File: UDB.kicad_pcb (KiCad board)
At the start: 4 copper layers, 18 x 16.5 mm, 14 parts, among them J1 TYPE-C-31-M12_13, J2 SM04B-SRSS-TB(LF)(SN), U1 TPD4E05U06DQAR

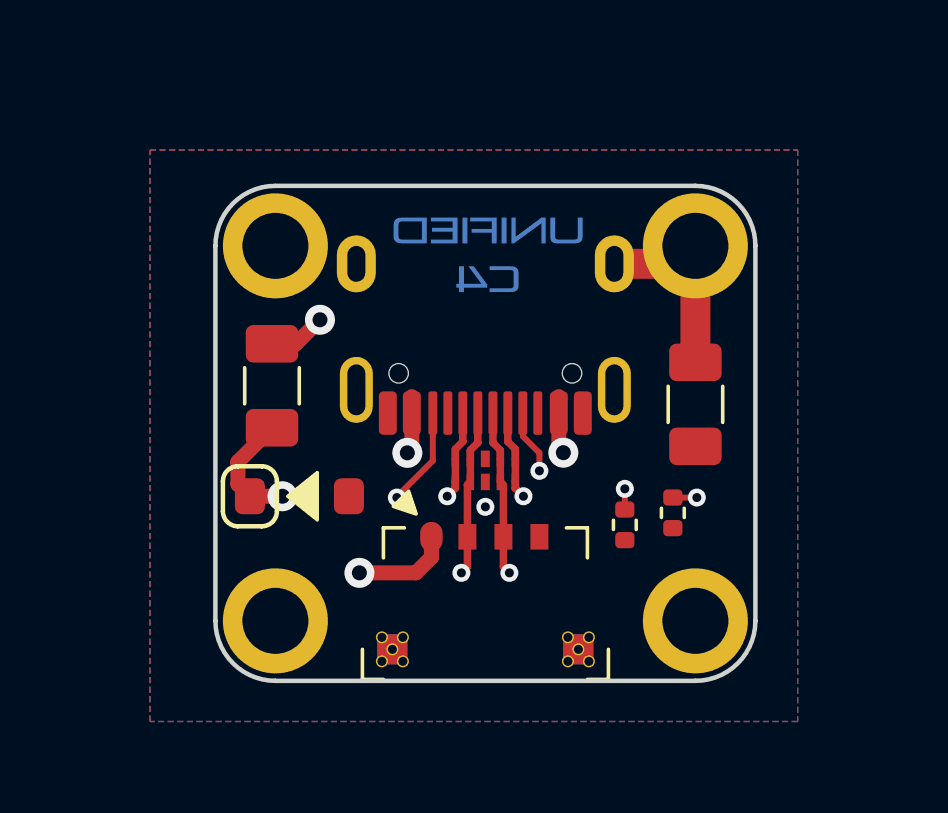
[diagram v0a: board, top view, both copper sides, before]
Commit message: Skew phase adjustment for outer USB diff pair
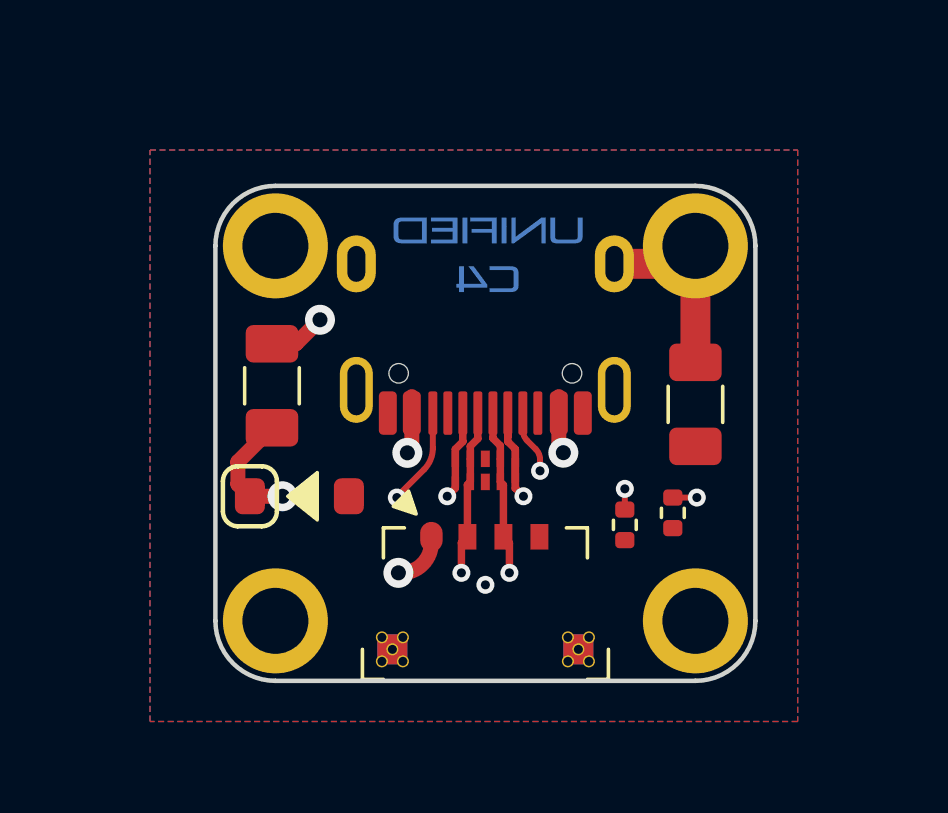
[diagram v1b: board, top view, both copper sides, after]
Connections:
- net DA+ renamed DP
- net DA- renamed DN
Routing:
- net DN: track 13.7 -> 18.8 mm
- net VBUS: track 18.7 -> 20.3 mm
- net DP: track 17.3 -> 16.7 mm

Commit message: Edit component metadata, final checks, release
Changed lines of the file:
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@@
   (title_block
     (title "Unified Daughterboard")
-    (date "2020-03-22")
-    (rev "C3")
-    (company "Designed by the keyboard community")
+    (date "2022-10-31")
+    (rev "C4-RC1")
+    (company "Designed by the UDB team")
   )
   (layers
@@
       (drillshape 0)
       (scaleselection 1)
-      (outputdirectory "../gerbers-C3")
+      (outputdirectory "./gerbers-C4")
     )
   )
@@
   (arc (start 69.324601 65.843) (mid 70.31455 66.25305) (end 71.3045 65.843) (width 0.5) (layer "In1.Cu") (net 9))
   (segment (start 66.7545 65.743) (end 66.7545 66.49) (width 0.5) (layer "F.Cu") (net 10))
+  (segment (start 71.621927 69.443) (end 72.2045 69.443) (width 0.5) (layer "F.Cu") (net 10))
   (segment (start 73.2045 68.443) (end 73.2045 68.243) (width 0.5) (layer "F.Cu") (net 10))
   (segment (start 67.8905 64.607) (end 66.7545 65.743) (width 0.5) (layer "F.Cu") (net 10))
   (segment (start 66.7545 66.49) (end 67.1545 66.89) (width 0.5) (layer "F.Cu") (net 10))
   (segment (start 67.1545 66.89) (end 68.2405 66.89) (width 0.5) (layer "F.Cu") (net 10))
-  (via (at 72.1045 69.443) (size 1) (drill 0.5) (layers "F.Cu" "B.Cu") (net 10))
+  (via (at 71.621927 69.443) (size 1) (drill 0.5) (layers "F.Cu" "B.Cu") (net 10))
   (via (at 68.2405 66.89) (size 1) (drill 0.5) (layers "F.Cu" "B.Cu") (net 10))
   (arc (start 72.2045 69.443) (mid 72.911607 69.150107) (end 73.2045 68.443) (width 0.5) (layer "F.Cu") (net 10))
   (segment (start 70.207713 68.857213) (end 68.2405 66.89) (width 0.5) (layer "In1.Cu") (net 10))
-  (segment (start 72.2045 69.443) (end 71.621927 69.443) (width 0.5) (layer "In1.Cu") (net 10))
   (arc (start 70.207713 68.857213) (mid 70.85656 69.290759) (end 71.621927 69.443) (width 0.5) (layer "In1.Cu") (net 10))
   (zone (net 0) (net_name "") (layers "F.Cu" "F.Fab") (hatch edge 0.508)

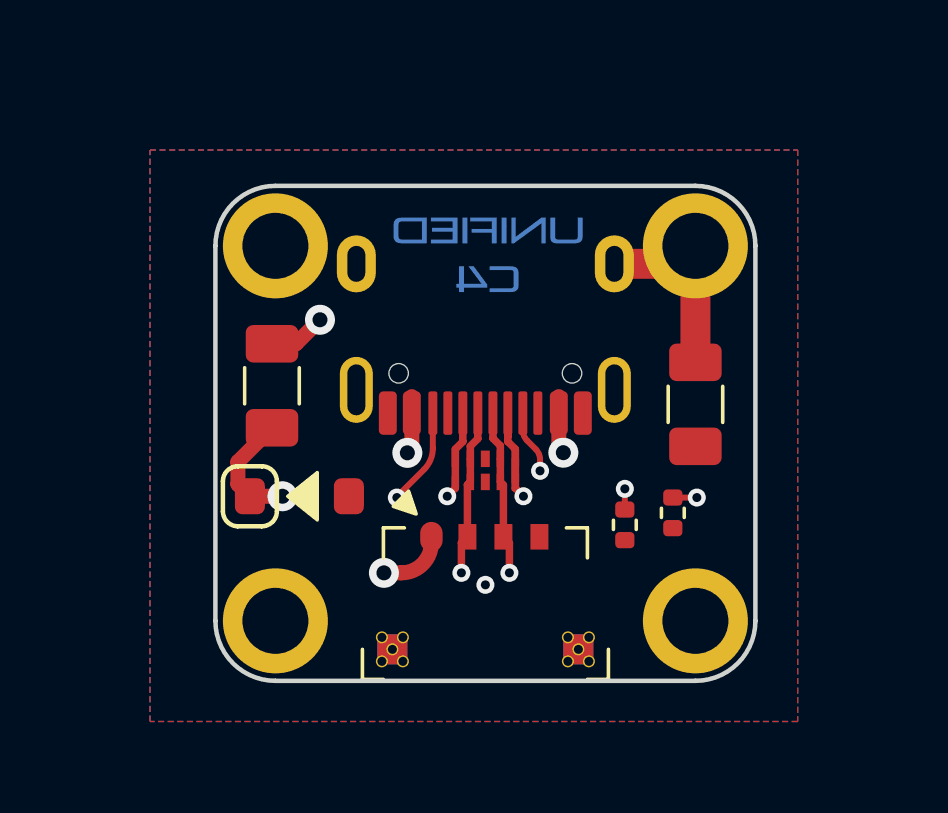
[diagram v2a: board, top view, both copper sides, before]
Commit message: Swap footprint
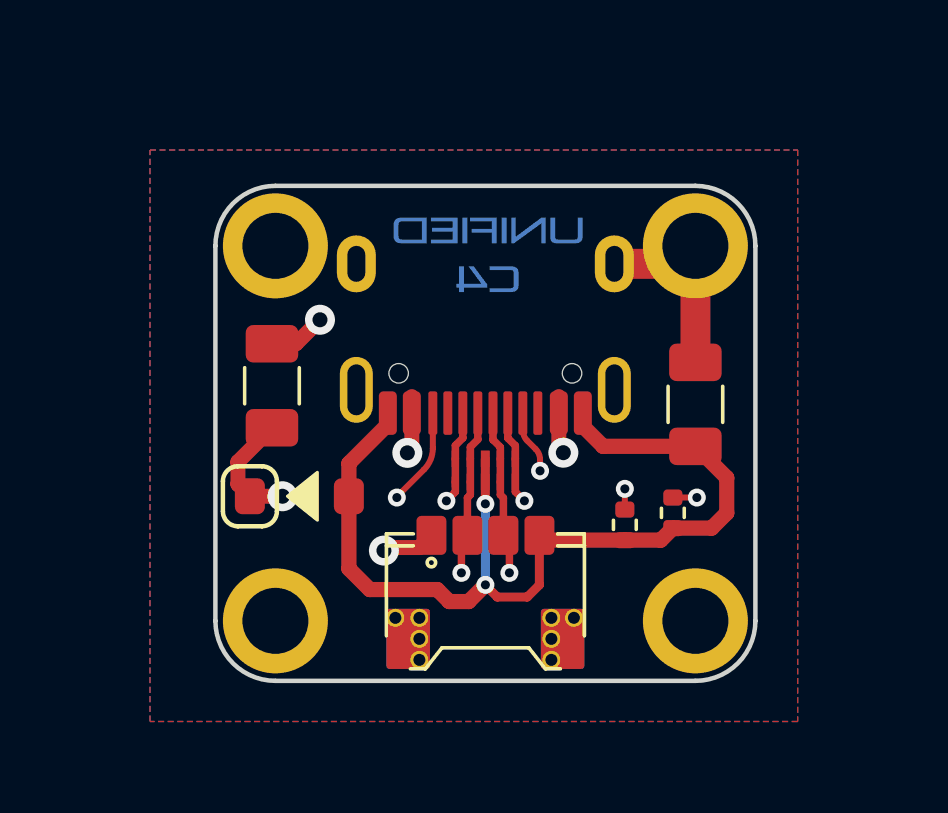
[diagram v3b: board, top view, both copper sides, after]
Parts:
- J2: value SM04B-SRSS-TB(LF)(SN) -> X1224WRS-04-LPV01; footprint acheron_Connectors:MOLEX_781710004_MountingReliefs -> locallib:PicoEZMate-Reinforced-Alt
- moved J2 1.90 mm to (75.0, 70.1)
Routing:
- net GND: track 0.00 -> 32.0 mm, vias 1 -> 2
- net DN: track 18.8 -> 16.8 mm
- net VCOM: track 10.7 -> 9.93 mm

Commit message: Retune trace thickness and USB data phase skew; plate connector mounting points to GND signal
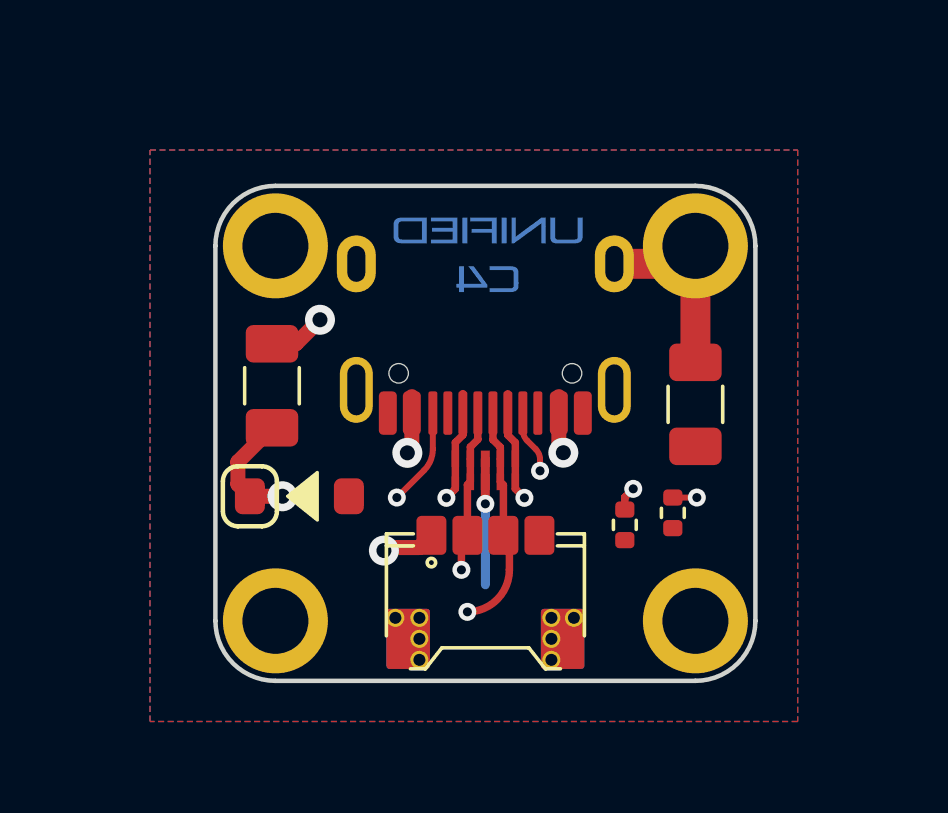
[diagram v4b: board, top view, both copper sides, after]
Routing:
- net GND: track 32.0 -> 4.20 mm, vias 2 -> 1
- net VBUS: track 20.3 -> 19.4 mm

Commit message: Add 4.1 silkscreen indicators to PCB
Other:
- rule pad_to_mask_clearance: 0.051 -> 0
- board text added: "V4.1"
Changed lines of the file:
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@@
       (dielectric_constraints no)
     )
-    (pad_to_mask_clearance 0.051)
-    (solder_mask_min_width 0.25)
+    (pad_to_mask_clearance 0)
     (grid_origin 95.8825 79.79)
     (pcbplotparams
@@
       (drillshape 0)
       (scaleselection 1)
-      (outputdirectory "./gerbers-C4")
+      (outputdirectory "gerber")
     )
   )
@@
     (pad "" smd roundrect (at -2.95 2) (size 0.7 1) (layers "F.Paste" "F.Mask") (roundrect_rratio 0.1428571429))
     (pad "" smd roundrect (at -0.6 -2) (size 0.75 1.2) (layers "F.Paste" "F.Mask") (roundrect_rratio 0.1666666667))
-    (pad "1" smd roundrect (at -1.8 -1.95) (size 1 1.3) (layers "F.Cu") (roundrect_rratio 0.1666666667)
+    (pad "1" smd roundrect (at -1.8 -1.95) (size 1 1.3) (layers "F.Cu") (roundrect_rratio 0.166667)
       (net 10 "VCOM") (pinfunction "Pin_1") (pintype "passive"))
-    (pad "2" smd roundrect (at -0.6 -1.95) (size 1 1.3) (layers "F.Cu") (roundrect_rratio 0.1666666667)
+    (pad "2" smd roundrect (at -0.6 -1.95) (size 1 1.3) (layers "F.Cu") (roundrect_rratio 0.166667)
       (net 8 "DN") (pinfunction "Pin_2") (pintype "passive"))
-    (pad "3" smd roundrect (at 0.6 -1.95) (size 1 1.3) (layers "F.Cu") (roundrect_rratio 0.1666666667)
+    (pad "3" smd roundrect (at 0.6 -1.95) (size 1 1.3) (layers "F.Cu") (roundrect_rratio 0.166667)
       (net 5 "DP") (pinfunction "Pin_3") (pintype "passive"))
-    (pad "4" smd roundrect (at 1.8 -1.95) (size 1 1.3) (layers "F.Cu") (roundrect_rratio 0.1666666667)
+    (pad "4" smd roundrect (at 1.8 -1.95) (size 1 1.3) (layers "F.Cu") (roundrect_rratio 0.166667)
       (net 1 "GND") (pinfunction "Pin_4") (pintype "passive"))
     (pad "MP" smd roundrect (at 2.575 1.5) (size 1.45 2) (layers "B.Cu") (roundrect_rratio 0.06896551724)
@@
   (gr_line (start 77.0045 67.043) (end 77.0045 68.543) (layer "F.CrtYd") (width 0.05))
   (gr_line (start 78.0045 72.543) (end 72.0045 72.543) (layer "F.CrtYd") (width 0.05))
+  (gr_text "V4.1" (at 74.9625 61.08) (layer "B.SilkS")
+    (effects (font (size 0.5 0.5) (thickness 0.125)) (justify mirror))
+  )
   (dimension (type aligned) (layer "Dwgs.User")
     (pts (xy 84.0045 56.543) (xy 66.0045 56.543))

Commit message: New version files and pertaining prod files added
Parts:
- removed L1: 60R@100MHz, Inductor_SMD:L_1206_3216Metric
- J2: footprint locallib:PicoEZMate-Reinforced-Alt -> acheron_Connectors:SM04B-SRSS-TB(LF)(SN)_mounting-reliefs
- moved R1 2.13 mm to (80.7, 66.0)
- moved R2 2.13 mm to (82.3, 65.6)
- moved J2 1.35 mm to (75.0, 68.8)
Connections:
- J1 pad S: GNDPWR -> GND
- MH2 pad 1: GNDPWR -> GND
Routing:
- net GNDPWR: track 6.83 -> 0.00 mm
- net GND: track 4.20 -> 6.19 mm, vias 1 -> 4
- net Net-(J1-CC2): track 15.6 -> 17.4 mm
- net Net-(J1-CC1): track 6.78 -> 8.55 mm
- net VCOM: track 9.83 -> 10.4 mm
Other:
- board text added: "V4.2"
- board text removed: "V4.1"

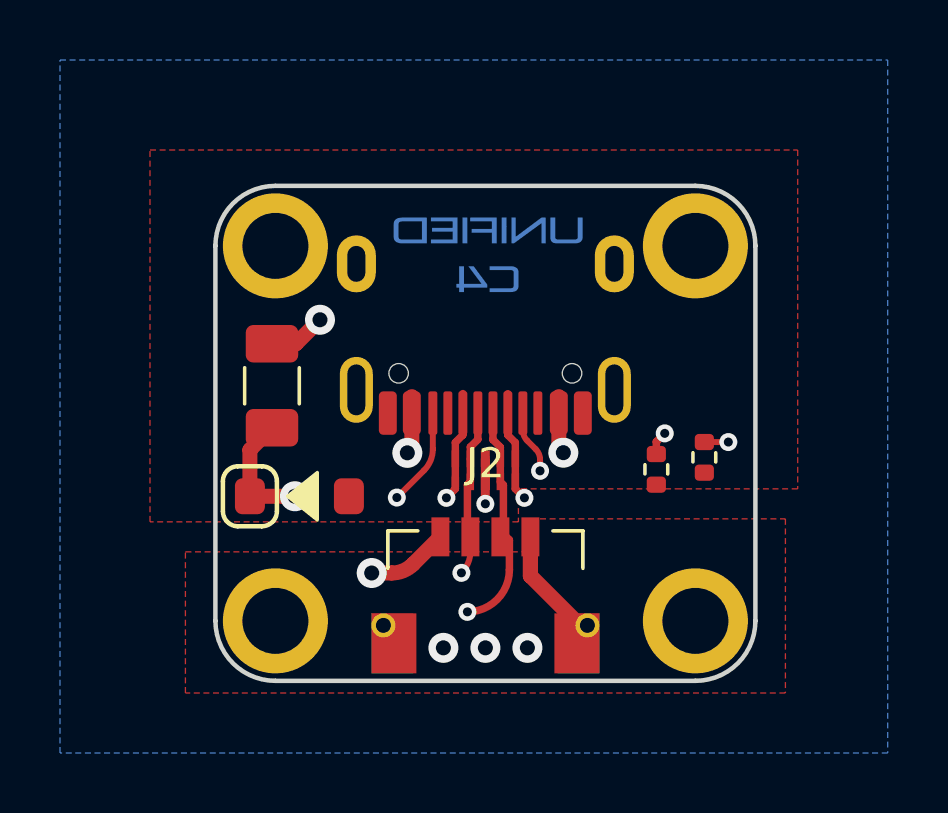
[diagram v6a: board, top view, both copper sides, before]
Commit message: Update logo to C5
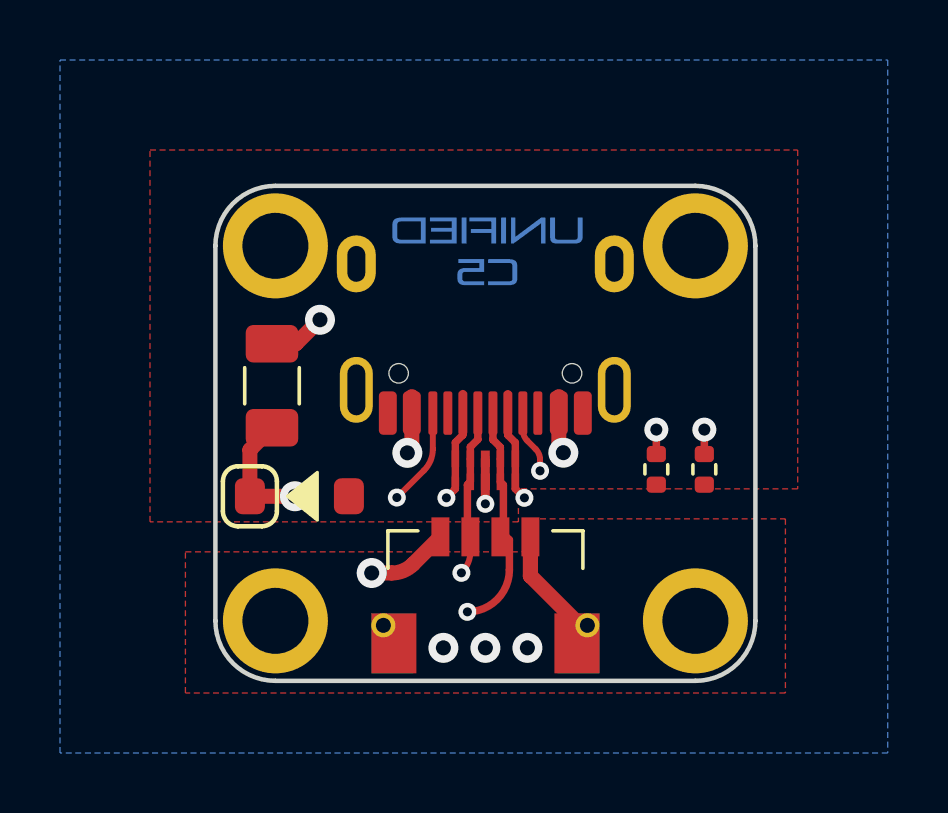
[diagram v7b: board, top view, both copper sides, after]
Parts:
- moved R2 0.40 mm to (82.3, 66.0)
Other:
- board text added: "V5.0"
- board text removed: "V4.2"

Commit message: Add `5.0-JSH` silkscreen marking
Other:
- board text added: "V5.0-JSH"
- board text removed: "V5.0"
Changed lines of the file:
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@@
   (gr_line (start 78.0045 72.543) (end 72.0045 72.543)
     (stroke (width 0.05) (type solid)) (layer "F.CrtYd"))
-  (gr_text "V5.0" (at 74.9625 61.08) (layer "B.SilkS")
-    (effects (font (size 0.5 0.5) (thickness 0.125)) (justify mirror))
+  (gr_text "V5.0-JSH" (at 74.9625 61.08) (layer "B.SilkS")
+    (effects (font (size 1 1) (thickness 0.2) bold) (justify mirror))
   )
   (dimension (type aligned) (layer "Dwgs.User")
